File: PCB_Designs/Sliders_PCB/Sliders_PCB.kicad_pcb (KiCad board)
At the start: 2 copper layers, 67.1 x 83.6 mm, 10 parts, among them P1 CONN_02X05, P2 CONN_01X01, P3 CONN_01X01, P4 CONN_01X01, P5 CONN_01X01

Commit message: Manufacture files added
* Gerbers created
* Drillfiles created
* G-CODE generated (milling information)
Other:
- board size 67.1 x 83.6 mm -> 67.4 x 83.6 mm
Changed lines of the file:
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@@
     (area 66.675 18.806699 189.865001 139.700001)
     (thickness 1.6)
-    (drawings 10)
+    (drawings 7)
     (tracks 89)
     (zones 0)
@@
   )
   (setup
-    (last_trace_width 1.5)
+    (last_trace_width 0.7)
     (user_trace_width 0.7)
     (user_trace_width 0.8)
@@
     (pad_drill 0.762)
     (pad_to_mask_clearance 0.2)
-    (aux_axis_origin 0 0)
-    (grid_origin 106.7308 101.9556)
+    (aux_axis_origin 98.9908 109.5756)
+    (grid_origin 98.9908 109.5756)
     (visible_elements 7FFFFFFF)
     (pcbplotparams
-      (layerselection 0x00000_00000001)
+      (layerselection 0x01000_80000001)
       (usegerberextensions false)
       (excludeedgelayer true)
@@
       (viasonmask false)
       (mode 1)
-      (useauxorigin false)
+      (useauxorigin true)
       (hpglpennumber 1)
       (hpglpenspeed 20)
@@
       (psnegative false)
       (psa4output false)
-      (plotreference true)
-      (plotvalue true)
+      (plotreference false)
+      (plotvalue false)
       (plotinvisibletext false)
       (padsonsilk false)
@@
       (drillshape 0)
       (scaleselection 1)
-      (outputdirectory ""))
+      (outputdirectory ../GERBERS/Sliders_PCB/))
   )
   (net 0 "")
@@
       (net 10 "Net-(P5-Pad1)"))
   )
-  (target plus (at 76.095017 25.913497) (size 5) (width 0.15) (layer Edge.Cuts))
-  (target plus (at 183.028766 26.0356) (size 5) (width 0.15) (layer Edge.Cuts))
-  (target plus (at 181.457411 109.60964) (size 5) (width 0.15) (layer Edge.Cuts))
   (dimension 83.435672 (width 0.3) (layer F.SilkS)
     (gr_text "83,436 mm" (at 171.834915 67.778236 90) (layer F.SilkS)
@@
     (arrow2b (pts (xy 109.382079 21.608134) (xy 110.502035 21.009302)))
   )
-  (gr_line (start 166.4208 26.0096) (end 99.3648 26.0096) (layer Edge.Cuts) (width 0.15))
+  (gr_line (start 166.4208 26.0096) (end 98.980796 26.0096) (layer Edge.Cuts) (width 0.15))
   (gr_line (start 166.4208 109.5756) (end 166.4208 26.0096) (layer Edge.Cuts) (width 0.15))
-  (gr_line (start 99.3648 109.5756) (end 166.4208 109.5756) (layer Edge.Cuts) (width 0.15))
-  (gr_line (start 99.3648 26.0096) (end 99.3648 109.5756) (layer Edge.Cuts) (width 0.15))
+  (gr_line (start 98.980794 109.5756) (end 166.4208 109.5756) (layer Edge.Cuts) (width 0.15))
+  (gr_line (start 98.9808 26.0056) (end 98.9808 109.575701) (layer Edge.Cuts) (width 0.15))
   (dimension 67.31 (width 0.3) (layer F.SilkS)
     (gr_text 67,310mm (at 132.715 24.685) (layer F.SilkS)

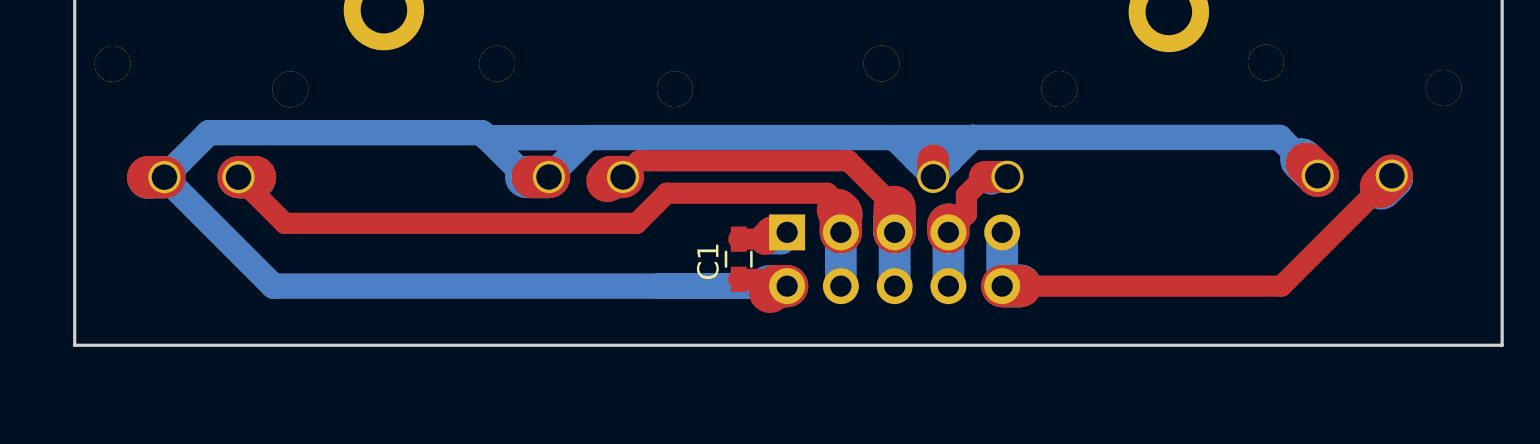
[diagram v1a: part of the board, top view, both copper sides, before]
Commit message: Hotfixes, updates and Photomask
* Edited small error in component placing (OLED_LCD)
* Updated all photomasks in light of recent events
* Generated photomask for OLED_LCD (.pdf)
* Updated all Gerberfiles (.gbr)
* Updated all drillfiles, now merging "plated" and unplated TH (.drl)
* With merge; all Non Plated Through Hole drills deleted (-NPTH.drl)
* Generated new G-CODE for all PCB (.ngc, .svg)
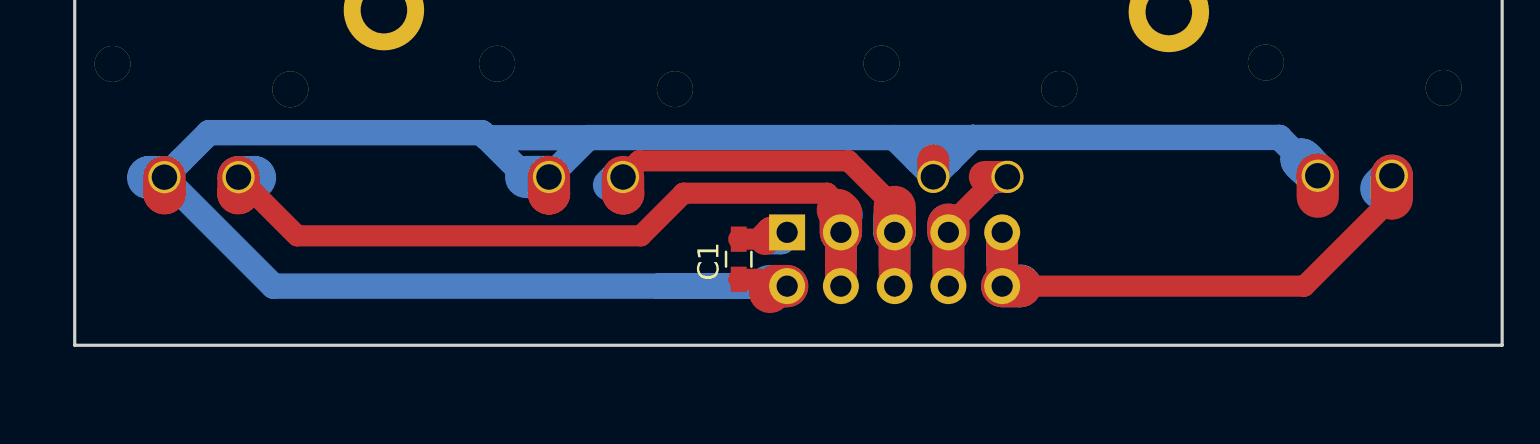
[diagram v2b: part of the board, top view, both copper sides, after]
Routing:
- net Net-(P1-Pad3): track 37.5 -> 39.7 mm
- net Net-(P1-Pad7): track 8.47 -> 10.1 mm
- net Net-(P1-Pad5): track 20.2 -> 21.8 mm
- net Net-(P1-Pad10): track 26.4 -> 27.8 mm
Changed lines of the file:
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@@
     (thickness 1.6)
     (drawings 7)
-    (tracks 89)
+    (tracks 93)
     (zones 0)
     (modules 10)
@@
   )
   (setup
-    (last_trace_width 0.7)
+    (last_trace_width 1.5)
     (user_trace_width 0.7)
     (user_trace_width 0.8)
@@
     (arrow2b (pts (xy 99.06 26.035) (xy 100.186504 25.448579)))
   )
+  (segment (start 157.7086 101.567) (end 157.7086 102.5578) (width 2) (layer F.Cu) (net 1))
+  (segment (start 121.3866 101.6254) (end 121.3866 102.4014) (width 2) (layer F.Cu) (net 1))
+  (segment (start 121.3866 102.4014) (end 121.3908 102.4056) (width 2) (layer F.Cu) (net 1))
+  (segment (start 103.2192 101.6334) (end 103.2192 102.384) (width 2) (layer F.Cu) (net 1))
+  (segment (start 103.2192 102.384) (end 103.2308 102.3956) (width 2) (layer F.Cu) (net 1))
   (segment (start 132.6388 106.7816) (end 132.1048 106.7816) (width 2) (layer F.Cu) (net 1))
   (segment (start 132.1048 106.7816) (end 131.8308 107.0556) (width 2) (layer F.Cu) (net 1))
   (segment (start 132.6388 106.7816) (end 131.7908 106.7816) (width 2) (layer B.Cu) (net 1))
   (segment (start 157.7086 101.567) (end 157.7086 101.5134) (width 2) (layer F.Cu) (net 1))
-  (segment (start 157.7086 101.5134) (end 157.1908 100.9956) (width 2) (layer F.Cu) (net 1))
   (segment (start 157.7086 101.567) (end 156.946601 100.805001) (width 2) (layer B.Cu) (net 1))
   (segment (start 156.946601 100.805001) (end 157.1772 101.0356) (width 2) (layer B.Cu) (net 1))
@@
   (segment (start 139.5476 100.8488) (end 139.5508 100.8456) (width 1.5) (layer F.Cu) (net 1))
   (segment (start 121.3866 101.6254) (end 120.30897 101.6254) (width 2) (layer B.Cu) (net 1))
-  (segment (start 120.6306 101.6254) (end 120.6208 101.6156) (width 2) (layer F.Cu) (net 1))
-  (segment (start 121.3866 101.6254) (end 120.6306 101.6254) (width 2) (layer F.Cu) (net 1))
   (segment (start 103.981199 100.871401) (end 103.2192 101.6334) (width 1.2) (layer B.Cu) (net 1))
   (segment (start 105.319211 99.533389) (end 103.981199 100.871401) (width 1.2) (layer B.Cu) (net 1))
@@
   (segment (start 103.2192 101.6334) (end 102.483 101.6334) (width 2) (layer B.Cu) (net 1))
   (segment (start 102.483 101.6334) (end 102.4508 101.6656) (width 2) (layer B.Cu) (net 1))
-  (segment (start 103.2192 101.6334) (end 102.463 101.6334) (width 2) (layer F.Cu) (net 1))
-  (segment (start 102.463 101.6334) (end 102.4508 101.6456) (width 2) (layer F.Cu) (net 1))
   (segment (start 137.693199 99.763399) (end 141.402001 99.763399) (width 1.2) (layer B.Cu) (net 1))
   (segment (start 141.402001 99.763399) (end 141.409601 99.755799) (width 1.2) (layer B.Cu) (net 1))
@@
   (segment (start 132.6388 104.2416) (end 131.9208 104.2416) (width 1.5) (layer F.Cu) (net 2))
   (segment (start 131.9208 104.2416) (end 131.6008 104.5616) (width 1.5) (layer F.Cu) (net 2))
+  (segment (start 135.1788 104.2416) (end 135.1788 105.9036) (width 1.5) (layer B.Cu) (net 3))
+  (segment (start 135.1788 104.2416) (end 135.1788 106.7816) (width 1.5) (layer F.Cu) (net 3))
+  (segment (start 109.49141 104.40561) (end 107.481199 102.395399) (width 1) (layer F.Cu) (net 3))
+  (segment (start 125.729232 104.40561) (end 109.49141 104.40561) (width 1) (layer F.Cu) (net 3))
+  (segment (start 127.743243 102.391599) (end 125.729232 104.40561) (width 1) (layer F.Cu) (net 3))
+  (segment (start 134.53088 102.391599) (end 127.743243 102.391599) (width 1) (layer F.Cu) (net 3))
+  (segment (start 107.481199 102.395399) (end 106.7192 101.6334) (width 1) (layer F.Cu) (net 3))
+  (segment (start 135.1788 103.039519) (end 134.53088 102.391599) (width 1) (layer F.Cu) (net 3))
+  (segment (start 135.1788 104.2416) (end 135.1788 103.039519) (width 1) (layer F.Cu) (net 3))
+  (segment (start 106.7192 101.6334) (end 106.7192 102.3772) (width 2) (layer F.Cu) (net 3))
+  (segment (start 106.7192 102.3772) (end 106.7008 102.3956) (width 2) (layer F.Cu) (net 3))
   (segment (start 135.1788 104.2416) (end 135.1788 103.327959) (width 2) (layer F.Cu) (net 3))
   (segment (start 135.1788 103.327959) (end 135.03458 103.183739) (width 2) (layer F.Cu) (net 3))
   (segment (start 135.1788 104.2416) (end 135.1788 103.4276) (width 2) (layer B.Cu) (net 3))
   (segment (start 135.1788 103.4276) (end 135.2108 103.3956) (width 2) (layer B.Cu) (net 3))
-  (segment (start 135.1788 104.2416) (end 135.1788 106.7816) (width 1.5) (layer B.Cu) (net 3))
-  (segment (start 108.90141 103.81561) (end 107.481199 102.395399) (width 1) (layer F.Cu) (net 3))
-  (segment (start 125.524832 103.81561) (end 108.90141 103.81561) (width 1) (layer F.Cu) (net 3))
-  (segment (start 126.948843 102.391599) (end 125.524832 103.81561) (width 1) (layer F.Cu) (net 3))
-  (segment (start 107.481199 102.395399) (end 106.7192 101.6334) (width 1) (layer F.Cu) (net 3))
-  (segment (start 134.53088 102.391599) (end 126.948843 102.391599) (width 1) (layer F.Cu) (net 3))
-  (segment (start 135.1788 103.039519) (end 134.53088 102.391599) (width 1) (layer F.Cu) (net 3))
-  (segment (start 135.1788 104.2416) (end 135.1788 103.039519) (width 1) (layer F.Cu) (net 3))
-  (segment (start 106.7192 101.6334) (end 107.4886 101.6334) (width 2) (layer F.Cu) (net 3))
-  (segment (start 107.4886 101.6334) (end 107.5008 101.6456) (width 2) (layer F.Cu) (net 3))
   (segment (start 106.7192 101.6334) (end 107.4686 101.6334) (width 2) (layer B.Cu) (net 3))
   (segment (start 107.4686 101.6334) (end 107.5008 101.6656) (width 2) (layer B.Cu) (net 3))
+  (segment (start 137.7188 104.2416) (end 137.7188 105.8836) (width 1.5) (layer B.Cu) (net 4))
+  (segment (start 137.7188 104.2416) (end 137.7188 106.7816) (width 1.5) (layer F.Cu) (net 4))
+  (segment (start 124.8866 102.3914) (end 124.9008 102.4056) (width 2) (layer F.Cu) (net 4))
+  (segment (start 124.8866 101.6254) (end 124.8866 102.3914) (width 2) (layer F.Cu) (net 4))
   (segment (start 137.710809 103.485609) (end 137.710809 104.233609) (width 2) (layer B.Cu) (net 4))
   (segment (start 137.710809 104.233609) (end 137.7188 104.2416) (width 2) (layer B.Cu) (net 4))
   (segment (start 137.7188 104.2416) (end 137.7188 103.039519) (width 2) (layer F.Cu) (net 4))
-  (segment (start 137.7188 104.2416) (end 137.7188 106.7816) (width 1.5) (layer B.Cu) (net 4))
-  (segment (start 124.8866 101.6254) (end 124.331 101.6254) (width 2) (layer F.Cu) (net 4))
-  (segment (start 124.331 101.6254) (end 124.1408 101.8156) (width 2) (layer F.Cu) (net 4))
   (segment (start 124.8866 101.6254) (end 124.591 101.6254) (width 1.5) (layer B.Cu) (net 4))
   (segment (start 124.591 101.6254) (end 124.2108 102.0056) (width 1.5) (layer B.Cu) (net 4))
@@
   (segment (start 125.648599 100.863401) (end 124.8866 101.6254) (width 1) (layer F.Cu) (net 4))
   (segment (start 135.542682 100.863401) (end 125.648599 100.863401) (width 1) (layer F.Cu) (net 4))
+  (segment (start 140.2588 104.2416) (end 140.2588 105.8976) (width 1.5) (layer B.Cu) (net 5))
+  (segment (start 140.2588 104.2416) (end 140.2588 106.7816) (width 1.5) (layer F.Cu) (net 5))
+  (segment (start 141.96997 102.241988) (end 141.96997 101.6178) (width 1) (layer F.Cu) (net 5))
+  (segment (start 140.2588 103.953158) (end 141.96997 102.241988) (width 1) (layer F.Cu) (net 5))
+  (segment (start 140.2588 104.2416) (end 140.2588 103.953158) (width 1) (layer F.Cu) (net 5))
   (segment (start 143.0476 101.6178) (end 141.96997 101.6178) (width 1.5) (layer F.Cu) (net 5))
   (segment (start 143.0476 101.6178) (end 142.3886 101.6178) (width 1.5) (layer B.Cu) (net 5))
@@
   (segment (start 140.2588 104.2416) (end 140.2588 103.879801) (width 2) (layer B.Cu) (net 5))
   (segment (start 140.2588 104.2416) (end 140.2588 103.879801) (width 2) (layer F.Cu) (net 5))
-  (segment (start 140.2588 104.2416) (end 140.2588 106.7816) (width 1.5) (layer B.Cu) (net 5))
-  (segment (start 140.2588 104.2416) (end 141.108799 103.391601) (width 1) (layer F.Cu) (net 5))
-  (segment (start 141.108799 103.391601) (end 141.108799 102.478971) (width 1) (layer F.Cu) (net 5))
-  (segment (start 141.108799 102.478971) (end 141.96997 101.6178) (width 1) (layer F.Cu) (net 5))
+  (segment (start 142.7988 104.2416) (end 142.7988 105.7336) (width 1.5) (layer B.Cu) (net 6))
+  (segment (start 142.7988 104.2416) (end 142.7988 106.7816) (width 1.5) (layer F.Cu) (net 6))
+  (segment (start 161.2086 101.567) (end 161.2086 102.64463) (width 2) (layer F.Cu) (net 6))
+  (segment (start 142.7988 106.7816) (end 157.07163 106.7816) (width 1) (layer F.Cu) (net 6))
+  (segment (start 157.07163 106.7816) (end 161.2086 102.64463) (width 1) (layer F.Cu) (net 6))
   (segment (start 142.7988 106.7816) (end 143.6348 106.7816) (width 2) (layer B.Cu) (net 6))
   (segment (start 143.6348 106.7816) (end 143.6608 106.7556) (width 2) (layer B.Cu) (net 6))
   (segment (start 142.7988 106.7816) (end 143.6608 106.7816) (width 2) (layer F.Cu) (net 6))
-  (segment (start 142.7988 106.7816) (end 142.7988 104.2416) (width 1.5) (layer B.Cu) (net 6))
   (segment (start 161.2086 101.567) (end 161.2086 101.6678) (width 2) (layer B.Cu) (net 6))
   (segment (start 161.2086 101.6678) (end 160.7108 102.1656) (width 2) (layer B.Cu) (net 6))
-  (segment (start 161.2086 101.567) (end 160.6908 102.0848) (width 2) (layer F.Cu) (net 6))
-  (segment (start 142.7988 106.7816) (end 155.994 106.7816) (width 1) (layer F.Cu) (net 6))
-  (segment (start 155.994 106.7816) (end 161.2086 101.567) (width 1) (layer F.Cu) (net 6))
   (zone (net 2) (net_name /GND) (layer F.Cu) (hatch edge 0.508)
     (connect_pads (clearance 0.508))
